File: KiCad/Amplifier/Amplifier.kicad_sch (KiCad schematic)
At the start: 25 parts, among them J1 Screw_Terminal_01x03, J2 Screw_Terminal_01x03, Q1 NPN, Q2 NPN, U1 TL074

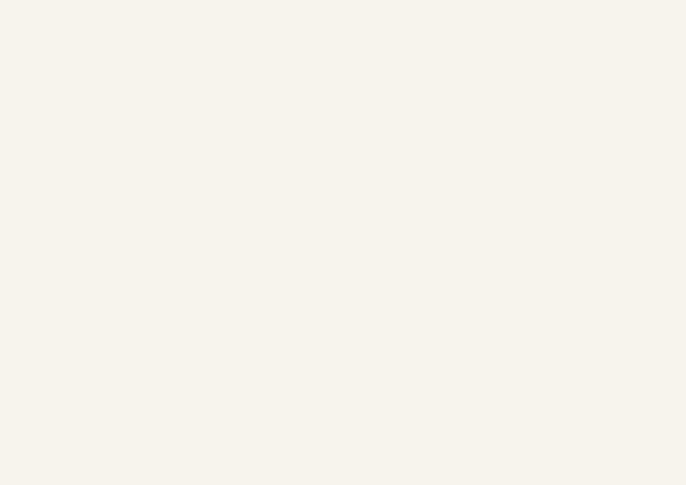
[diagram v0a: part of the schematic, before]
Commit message: added mounting holes to schematics, adjusted board sizes
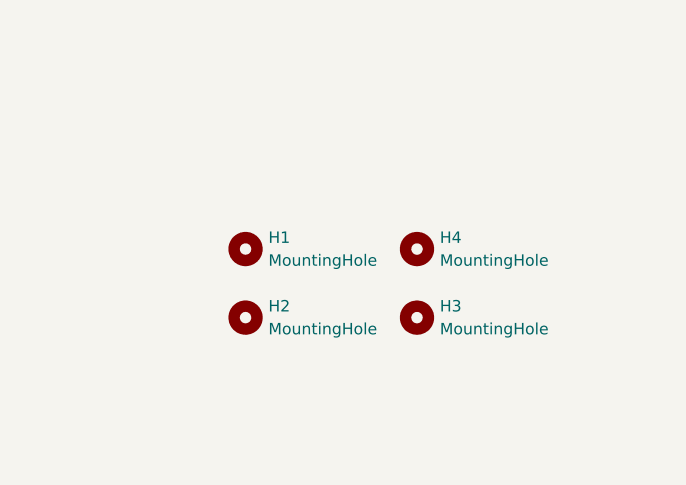
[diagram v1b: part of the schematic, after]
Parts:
- added H1, H2, H3, H4: MountingHole, MountingHole:MountingHole_3.2mm_M3, symbol Mechanical:MountingHole

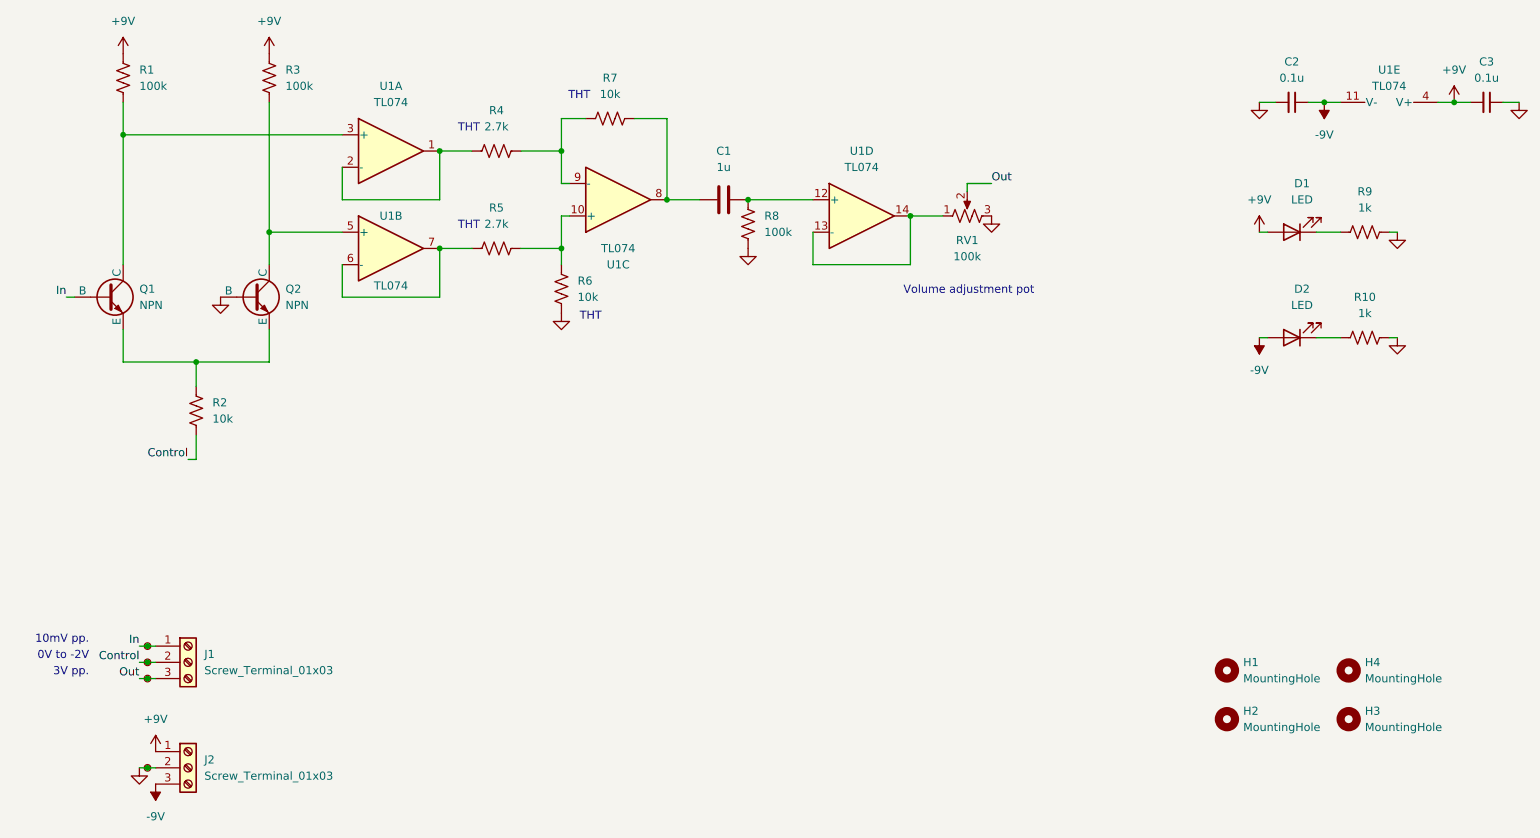
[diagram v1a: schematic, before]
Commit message: merged project into one combined board (excluding the buttons)
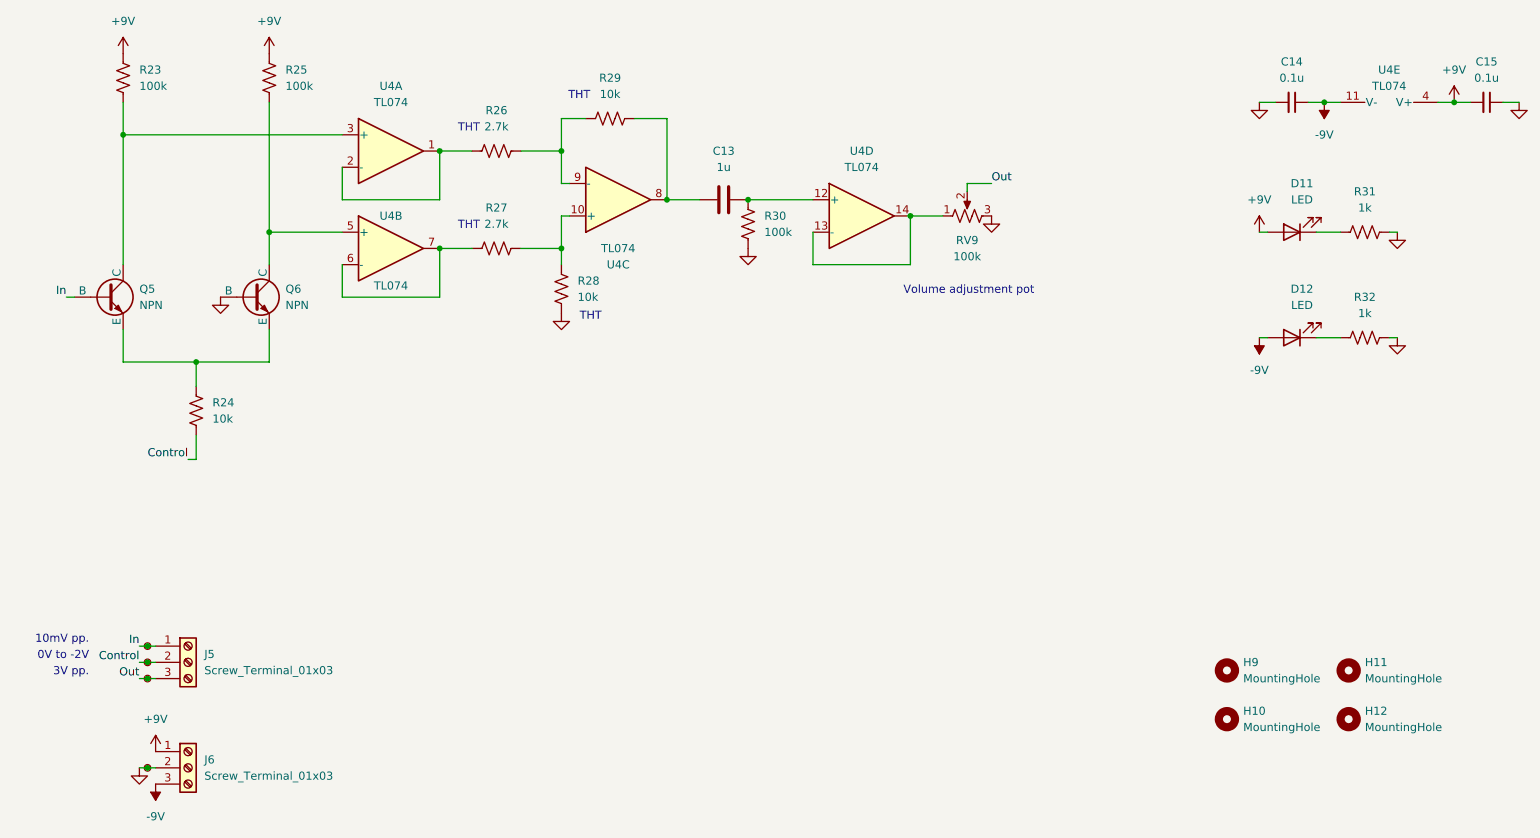
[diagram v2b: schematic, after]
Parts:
- renumbered C1 to C13, C2 to C14, C3 to C15, D1 to D11, D2 to D12, H2 to H10, H4 to H11, H3 to H12, H1 to H9, J1 to J5, J2 to J6, Q1 to Q5, Q2 to Q6, R1 to R23, R2 to R24, R3 to R25, R4 to R26, R5 to R27, R6 to R28, R7 to R29, R8 to R30, R9 to R31, R10 to R32, RV1 to RV9, TP1 to TP13, TP2 to TP14, TP3 to TP15, TP4 to TP16, U1 to U4
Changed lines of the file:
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@@
 		(dnp no)
 		(fields_autoplaced yes)
-		(property "Reference" "U1"
+		(property "Reference" "U4"
 			(at 146.05 44.45 0)
 			(show_name no)
@@
 			(project "Amplifier"
 				(path "/4b9119d6-fa5d-4921-8a56-e3e986a94725"
-					(reference "U1")
+					(reference "U4")
 					(unit 4)
 				)
@@
 		(dnp no)
 		(fields_autoplaced yes)
-		(property "Reference" "J2"
+		(property "Reference" "J6"
 			(at 43.18 139.6999 0)
 			(show_name no)
@@
 			(project "Amplifier"
 				(path "/4b9119d6-fa5d-4921-8a56-e3e986a94725"
-					(reference "J2")
+					(reference "J6")
 					(unit 1)
 				)
@@
 		(dnp no)
 		(fields_autoplaced yes)
-		(property "Reference" "R6"
+		(property "Reference" "R28"
 			(at 101.6 64.7699 0)
 			(show_name no)
@@
 			(project "Amplifier"
 				(path "/4b9119d6-fa5d-4921-8a56-e3e986a94725"
-					(reference "R6")
+					(reference "R28")
 					(unit 1)
 				)
@@
 		(dnp no)
 		(fields_autoplaced yes)
-		(property "Reference" "U1"
+		(property "Reference" "U4"
 			(at 228.6 31.75 90)
 			(show_name no)
@@
 			(project "Amplifier"
 				(path "/4b9119d6-fa5d-4921-8a56-e3e986a94725"
-					(reference "U1")
+					(reference "U4")
 					(unit 5)
 				)
@@
 		(dnp no)
 		(fields_autoplaced yes)
-		(property "Reference" "R9"
+		(property "Reference" "R31"
 			(at 224.79 50.8 90)
 			(show_name no)
@@
 			(project "Amplifier"
 				(path "/4b9119d6-fa5d-4921-8a56-e3e986a94725"
-					(reference "R9")
+					(reference "R31")
 					(unit 1)
 				)
@@
 		(dnp no)
 		(fields_autoplaced yes)
-		(property "Reference" "J1"
+		(property "Reference" "J5"
 			(at 43.18 123.1899 0)
 			(show_name no)
@@
 			(project "Amplifier"
 				(path "/4b9119d6-fa5d-4921-8a56-e3e986a94725"
-					(reference "J1")
+					(reference "J5")
 					(unit 1)
 				)
@@
 		(dnp no)
 		(fields_autoplaced yes)
-		(property "Reference" "TP1"
+		(property "Reference" "TP13"
 			(at 35.56 120.6499 0)
 			(hide yes)
@@
 			(project "Amplifier"
 				(path "/4b9119d6-fa5d-4921-8a56-e3e986a94725"
-					(reference "TP1")
+					(reference "TP13")
 					(unit 1)
 				)
@@
 		(dnp no)
 		(fields_autoplaced yes)
-		(property "Reference" "TP3"
+		(property "Reference" "TP15"
 			(at 35.56 125.7299 0)
 			(hide yes)
@@
 			(project "Amplifier"
 				(path "/4b9119d6-fa5d-4921-8a56-e3e986a94725"
-					(reference "TP3")
+					(reference "TP15")
 					(unit 1)
 				)
@@
 		(dnp no)
 		(fields_autoplaced yes)
-		(property "Reference" "R8"
+		(property "Reference" "R30"
 			(at 130.81 54.6099 0)
 			(show_name no)
@@
 			(project "Amplifier"
 				(path "/4b9119d6-fa5d-4921-8a56-e3e986a94725"
-					(reference "R8")
+					(reference "R30")
 					(unit 1)
 				)
@@
 		(dnp no)
 		(fields_autoplaced yes)
-		(property "Reference" "H3"
+		(property "Reference" "H12"
 			(at 224.79 132.0799 0)
 			(show_name no)
@@
 			(project "Amplifier"
 				(path "/4b9119d6-fa5d-4921-8a56-e3e986a94725"
-					(reference "H3")
+					(reference "H12")
 					(unit 1)
 				)
@@
 		(dnp no)
 		(fields_autoplaced yes)
-		(property "Reference" "R2"
+		(property "Reference" "R24"
 			(at 44.45 83.8199 0)
 			(show_name no)
@@
 			(project "Amplifier"
 				(path "/4b9119d6-fa5d-4921-8a56-e3e986a94725"
-					(reference "R2")
+					(reference "R24")
 					(unit 1)
 				)
@@
 		(dnp no)
 		(fields_autoplaced yes)
-		(property "Reference" "D1"
+		(property "Reference" "D11"
 			(at 214.9475 49.53 0)
 			(show_name no)
@@
 			(project "Amplifier"
 				(path "/4b9119d6-fa5d-4921-8a56-e3e986a94725"
-					(reference "D1")
+					(reference "D11")
 					(unit 1)
 				)
@@
 		(dnp no)
 		(fields_autoplaced yes)
-		(property "Reference" "U1"
+		(property "Reference" "U4"
 			(at 72.39 34.29 0)
 			(show_name no)
@@
 			(project "Amplifier"
 				(path "/4b9119d6-fa5d-4921-8a56-e3e986a94725"
-					(reference "U1")
+					(reference "U4")
 					(unit 1)
 				)
@@
 		(in_pos_files yes)
 		(dnp no)
-		(property "Reference" "U1"
+		(property "Reference" "U4"
 			(at 107.95 62.23 0)
 			(show_name no)
@@
 			(project "Amplifier"
 				(path "/4b9119d6-fa5d-4921-8a56-e3e986a94725"
-					(reference "U1")
+					(reference "U4")
 					(unit 3)
 				)
@@
 		(dnp no)
 		(fields_autoplaced yes)
-		(property "Reference" "TP2"
+		(property "Reference" "TP14"
 			(at 35.56 123.1899 0)
 			(hide yes)
@@
 			(project "Amplifier"
 				(path "/4b9119d6-fa5d-4921-8a56-e3e986a94725"
-					(reference "TP2")
+					(reference "TP14")
 					(unit 1)
 				)
@@
 		(dnp no)
 		(fields_autoplaced yes)
-		(property "Reference" "H1"
+		(property "Reference" "H9"
 			(at 205.74 124.4599 0)
 			(show_name no)
@@
 			(project "Amplifier"
 				(path "/4b9119d6-fa5d-4921-8a56-e3e986a94725"
-					(reference "H1")
+					(reference "H9")
 					(unit 1)
 				)
@@
 		(dnp no)
 		(fields_autoplaced yes)
-		(property "Reference" "C1"
+		(property "Reference" "C13"
 			(at 124.46 44.45 90)
 			(show_name no)
@@
 			(project "Amplifier"
 				(path "/4b9119d6-fa5d-4921-8a56-e3e986a94725"
-					(reference "C1")
+					(reference "C13")
 					(unit 1)
 				)
@@
 		(dnp no)
 		(fields_autoplaced yes)
-		(property "Reference" "R3"
+		(property "Reference" "R25"
 			(at 55.88 31.7499 0)
 			(show_name no)
@@
 			(project "Amplifier"
 				(path "/4b9119d6-fa5d-4921-8a56-e3e986a94725"
-					(reference "R3")
+					(reference "R25")
 					(unit 1)
 				)
@@
 		(dnp no)
 		(fields_autoplaced yes)
-		(property "Reference" "TP4"
+		(property "Reference" "TP16"
 			(at 35.56 139.6999 0)
 			(hide yes)
@@
 			(project "Amplifier"
 				(path "/4b9119d6-fa5d-4921-8a56-e3e986a94725"
-					(reference "TP4")
+					(reference "TP16")
 					(unit 1)
 				)
@@
 		(dnp no)
 		(fields_autoplaced yes)
-		(property "Reference" "H2"
+		(property "Reference" "H10"
 			(at 205.74 132.0799 0)
 			(show_name no)
@@
 			(project "Amplifier"
 				(path "/4b9119d6-fa5d-4921-8a56-e3e986a94725"
-					(reference "H2")
+					(reference "H10")
 					(unit 1)
 				)
@@
 		(dnp no)
 		(fields_autoplaced yes)
-		(property "Reference" "R7"
+		(property "Reference" "R29"
 			(at 106.68 33.02 90)
 			(show_name no)
@@
 			(project "Amplifier"
 				(path "/4b9119d6-fa5d-4921-8a56-e3e986a94725"
-					(reference "R7")
+					(reference "R29")
 					(unit 1)
 				)
@@
 		(dnp no)
 		(fields_autoplaced yes)
-		(property "Reference" "H4"
+		(property "Reference" "H11"
 			(at 224.79 124.4599 0)
 			(show_name no)
@@
 			(project "Amplifier"
 				(path "/4b9119d6-fa5d-4921-8a56-e3e986a94725"
-					(reference "H4")
+					(reference "H11")
 					(unit 1)
 				)
@@
 		(dnp no)
 		(fields_autoplaced yes)
-		(property "Reference" "R4"
+		(property "Reference" "R26"
 			(at 88.9 38.1 90)
 			(show_name no)
@@
 			(project "Amplifier"
 				(path "/4b9119d6-fa5d-4921-8a56-e3e986a94725"
-					(reference "R4")
+					(reference "R26")
 					(unit 1)
 				)
@@
 		(dnp no)
 		(fields_autoplaced yes)
-		(property "Reference" "C3"
+		(property "Reference" "C15"
 			(at 243.8336 30.48 90)
 			(show_name no)
@@
 			(project "Amplifier"
 				(path "/4b9119d6-fa5d-4921-8a56-e3e986a94725"
-					(reference "C3")
+					(reference "C15")
 					(unit 1)
 				)
@@
 		(dnp no)
 		(fields_autoplaced yes)
-		(property "Reference" "R10"
+		(property "Reference" "R32"
 			(at 224.79 67.31 90)
 			(show_name no)
@@
 			(project "Amplifier"
 				(path "/4b9119d6-fa5d-4921-8a56-e3e986a94725"
-					(reference "R10")
+					(reference "R32")
 					(unit 1)
 				)
@@
 		(dnp no)
 		(fields_autoplaced yes)
-		(property "Reference" "Q2"
+		(property "Reference" "Q6"
 			(at 55.88 66.0399 0)
 			(show_name no)
@@
 			(project "Amplifier"
 				(path "/4b9119d6-fa5d-4921-8a56-e3e986a94725"
-					(reference "Q2")
+					(reference "Q6")
 					(unit 1)
 				)
@@
 		(dnp no)
 		(fields_autoplaced yes)
-		(property "Reference" "D2"
+		(property "Reference" "D12"
 			(at 214.9475 66.04 0)
 			(show_name no)
@@
 			(project "Amplifier"
 				(path "/4b9119d6-fa5d-4921-8a56-e3e986a94725"
-					(reference "D2")
+					(reference "D12")
 					(unit 1)
 				)
@@
 		(dnp no)
 		(fields_autoplaced yes)
-		(property "Reference" "C2"
+		(property "Reference" "C14"
 			(at 213.3536 30.48 90)
 			(show_name no)
@@
 			(project "Amplifier"
 				(path "/4b9119d6-fa5d-4921-8a56-e3e986a94725"
-					(reference "C2")
+					(reference "C14")
 					(unit 1)
 				)
@@
 		(dnp no)
 		(fields_autoplaced yes)
-		(property "Reference" "R5"
+		(property "Reference" "R27"
 			(at 88.9 53.34 90)
 			(show_name no)
@@
 			(project "Amplifier"
 				(path "/4b9119d6-fa5d-4921-8a56-e3e986a94725"
-					(reference "R5")
+					(reference "R27")
 					(unit 1)
 				)
@@
 		(in_pos_files yes)
 		(dnp no)
-		(property "Reference" "U1"
+		(property "Reference" "U4"
 			(at 72.39 54.61 0)
 			(show_name no)
@@
 			(project "Amplifier"
 				(path "/4b9119d6-fa5d-4921-8a56-e3e986a94725"
-					(reference "U1")
+					(reference "U4")
 					(unit 2)
 				)
@@
 		(dnp no)
 		(fields_autoplaced yes)
-		(property "Reference" "R1"
+		(property "Reference" "R23"
 			(at 33.02 31.7499 0)
 			(show_name no)
@@
 			(project "Amplifier"
 				(path "/4b9119d6-fa5d-4921-8a56-e3e986a94725"
-					(reference "R1")
+					(reference "R23")
 					(unit 1)
 				)
@@
 		(dnp no)
 		(fields_autoplaced yes)
-		(property "Reference" "Q1"
+		(property "Reference" "Q5"
 			(at 33.02 66.0399 0)
 			(show_name no)
@@
 			(project "Amplifier"
 				(path "/4b9119d6-fa5d-4921-8a56-e3e986a94725"
-					(reference "Q1")
+					(reference "Q5")
 					(unit 1)
 				)
@@
 		(dnp no)
 		(fields_autoplaced yes)
-		(property "Reference" "RV1"
+		(property "Reference" "RV9"
 			(at 162.56 58.42 90)
 			(show_name no)
@@
 			(project "Amplifier"
 				(path "/4b9119d6-fa5d-4921-8a56-e3e986a94725"
-					(reference "RV1")
+					(reference "RV9")
 					(unit 1)
 				)
